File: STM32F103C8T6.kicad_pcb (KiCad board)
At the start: 2 copper layers, 40 x 33 mm, 33 parts, among them J1 MICROXNJ, J2 Conn_01x04_Pin, J3 Conn_01x04_Pin, J4 Conn_01x04_Pin, SW1 SW_SPDT, U1 STM32F103C8T6, U2 AMS1117-3.3, Y1 16MHz

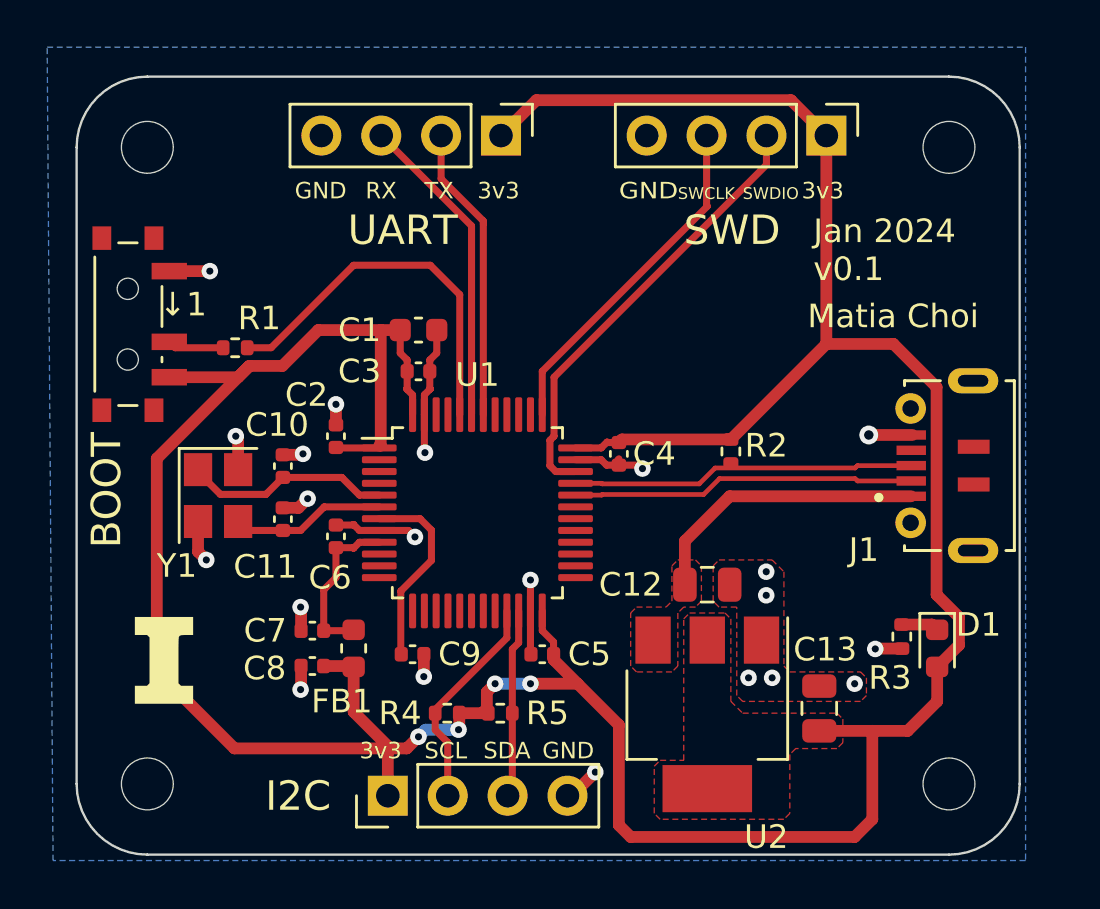
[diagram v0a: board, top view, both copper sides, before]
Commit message: changed footprint of the ferrite bead
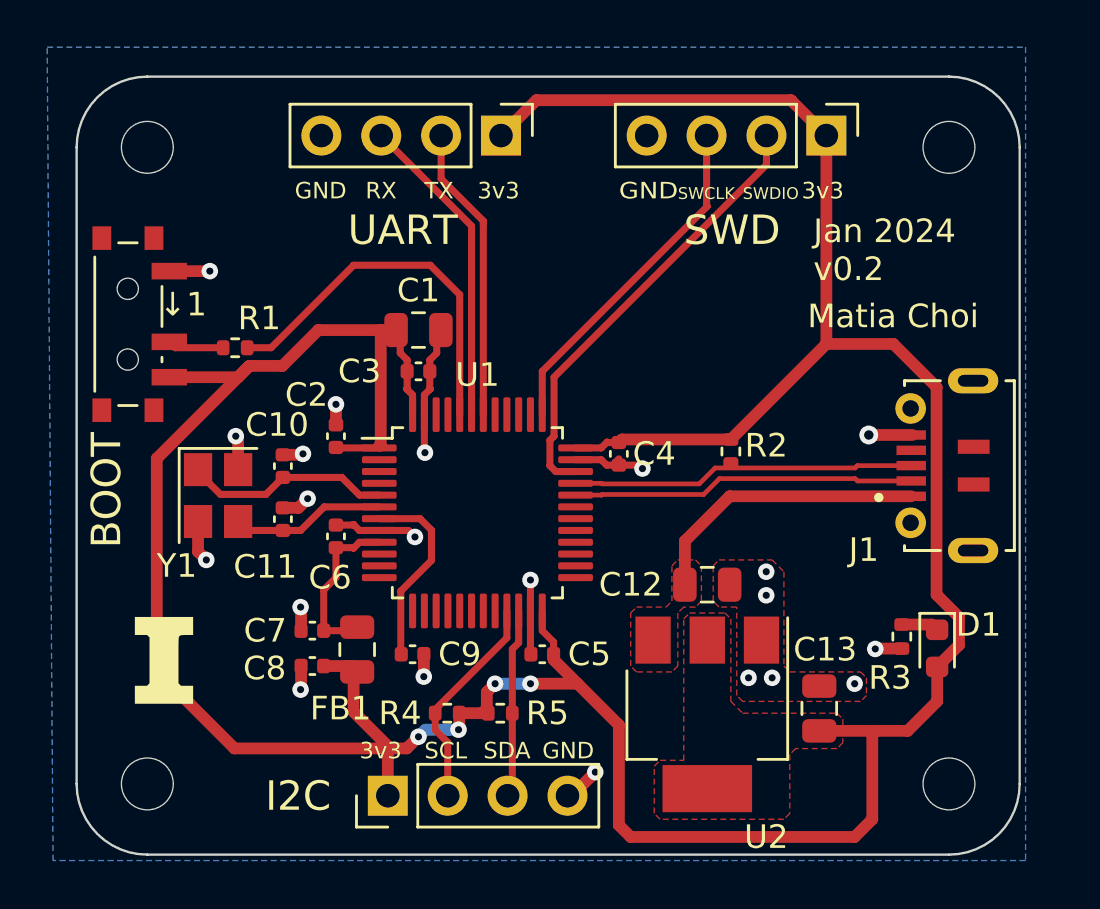
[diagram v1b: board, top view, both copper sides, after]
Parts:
- C1: footprint Capacitor_SMD:C_0603_1608Metric -> Capacitor_SMD:C_0805_2012Metric
- FB1: footprint Inductor_SMD:L_0603_1608Metric -> Capacitor_SMD:C_0805_2012Metric
- moved FB1 0.16 mm to (99.9, 90.8)
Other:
- board text added: "Jan 2024 v0.2"
- board text added: "STM32F103C8T6 Test Board v0.2 Jan 2024 by Matia Choi Github: matia6170"
- board text removed: "Jan 2024 v0.1"
- board text removed: "STM32F103C8T6 Test Board Jan 2024 by Matia Choi Github: matia6170"
